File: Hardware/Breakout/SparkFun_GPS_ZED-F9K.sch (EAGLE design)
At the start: 83 parts, among them J1 U.FL, J3 QWIIC_RIGHT_ANGLE, J4 QWIIC_RIGHT_ANGLE, U1 UBLOX_ZED_F9R, U2 3.3V, U4 HCPL-270L

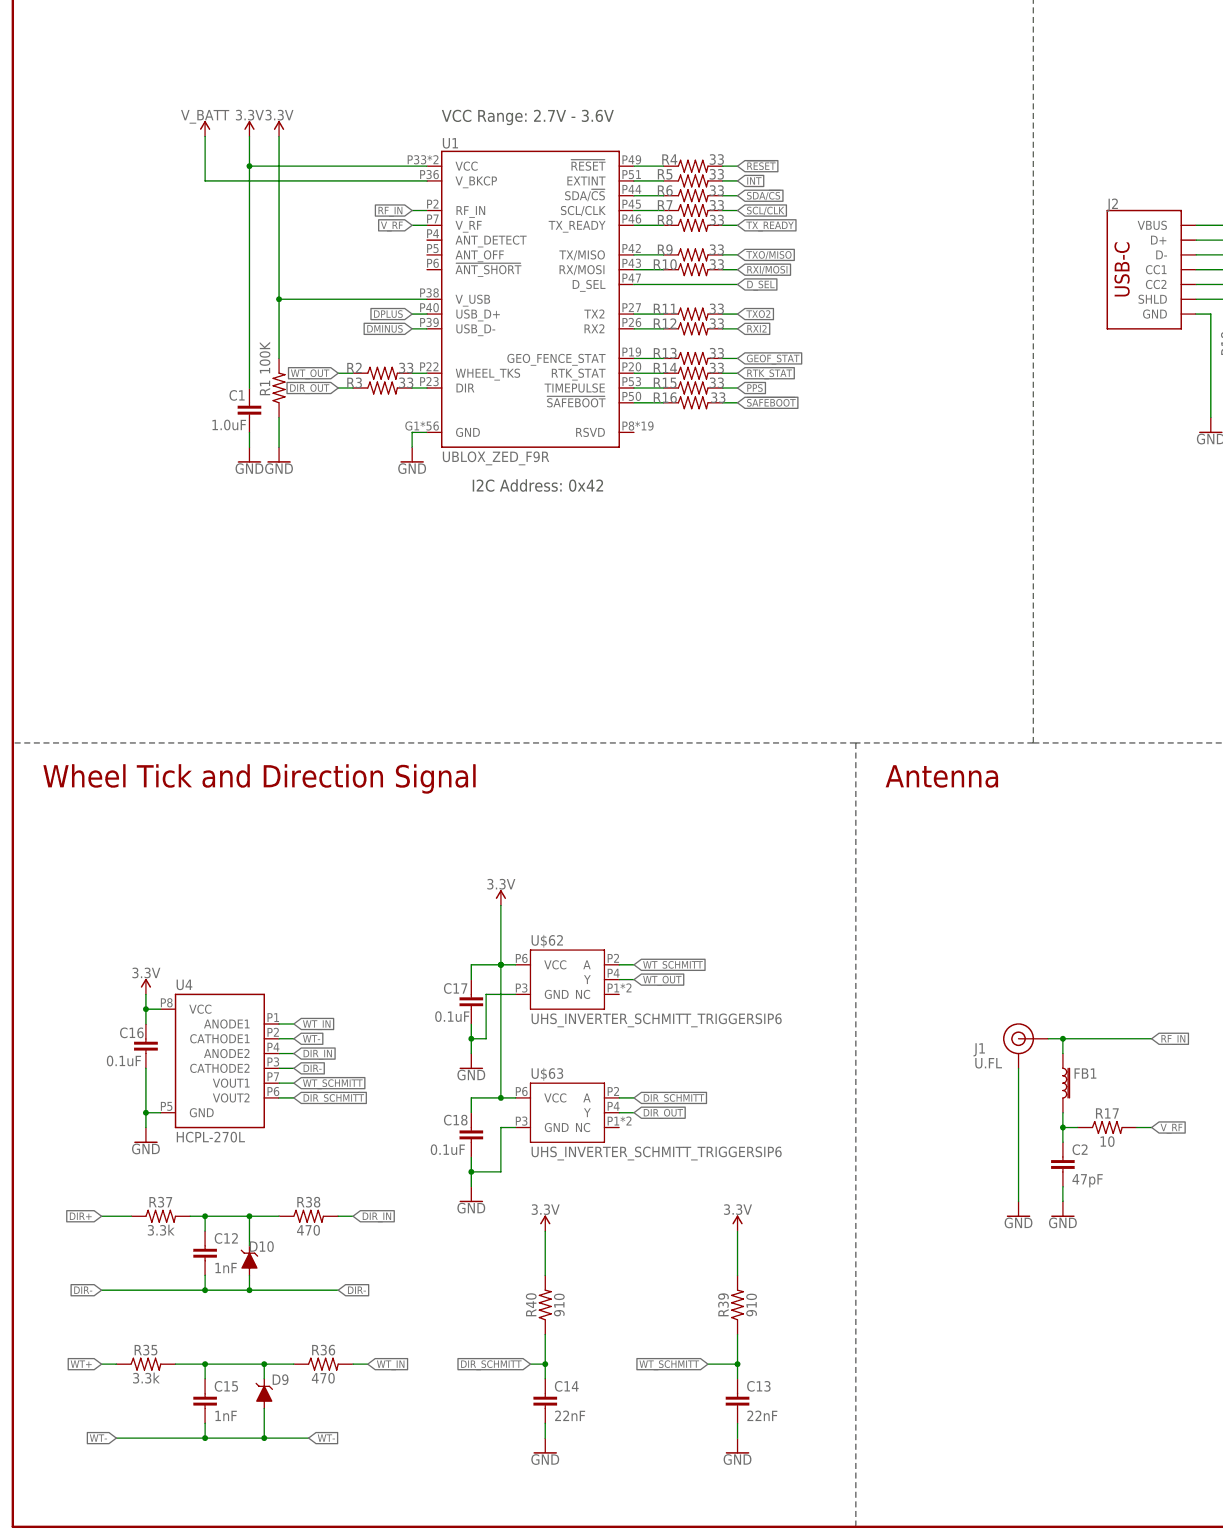
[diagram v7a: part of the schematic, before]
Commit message: Removes gerbers, removes caps from schmitt trigger on both designs, adds 1uF cap to V_USB on breakout
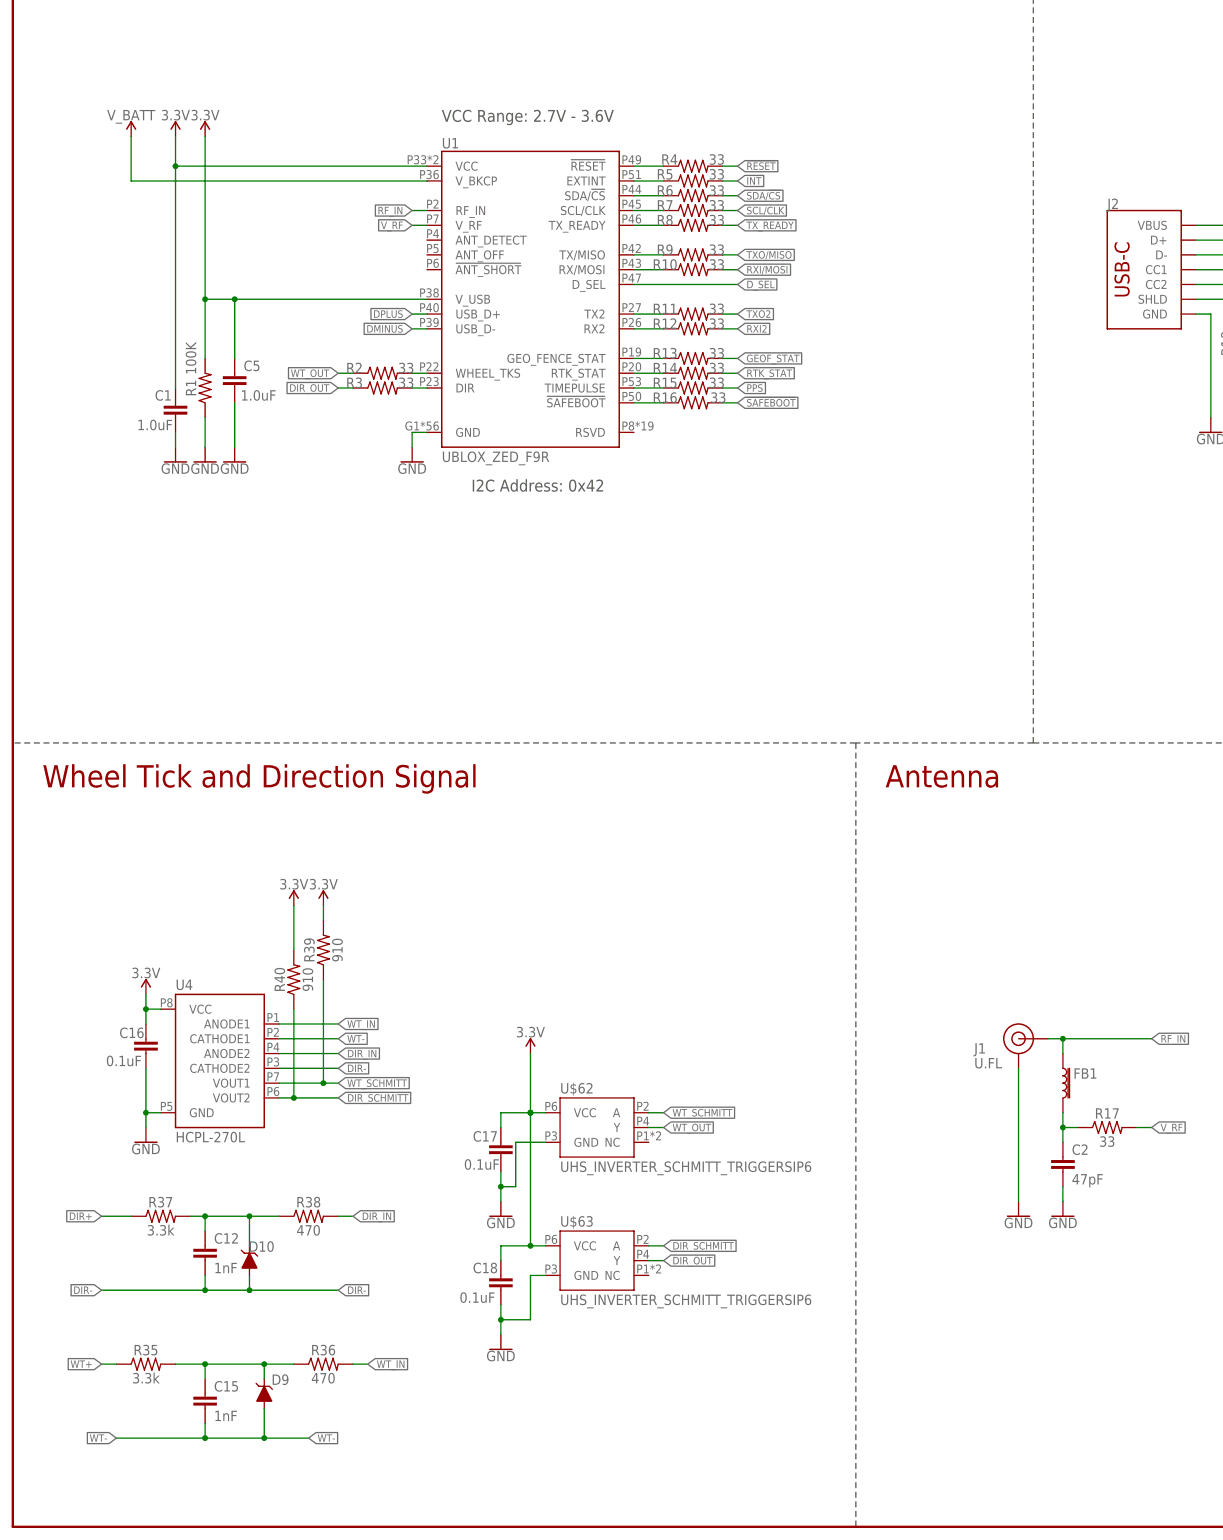
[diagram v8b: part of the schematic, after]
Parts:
- removed C13, C14: 22nF, SparkFun-Capacitors:22NF/22,000PF-0603-25V-10%-X7R
- added C5: 1.0uF, SparkFun-Capacitors:1.0UF-0603-16V-10%-X7R
- FB1: value FERRITE_BEAD-120_OHM-0402 -> 120NH; device SparkFun-Coils:FERRITE_BEAD-120_OHM-0402 -> SparkFun-Coils:FERRITE_BEAD_GNSS
- R17: value 10 -> 33; device SparkFun-Resistors:10OHM-0603-1/10W-1% -> SparkFun-Resistors:33OHM-0603-1/10W-1%
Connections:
- net 3.3V: now also C5.1
- net DIR_SCHMITT: no longer C14.1
- net GND: now also C5.2; no longer C13.2, C14.2
- net WT_SCHMITT: no longer C13.1
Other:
- moved on the sheet: C1, C17, C18, R1, R39, R40, U$62, U$63
